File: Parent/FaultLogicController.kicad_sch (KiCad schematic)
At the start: 4 parts, among them U57 4072, U60 4071

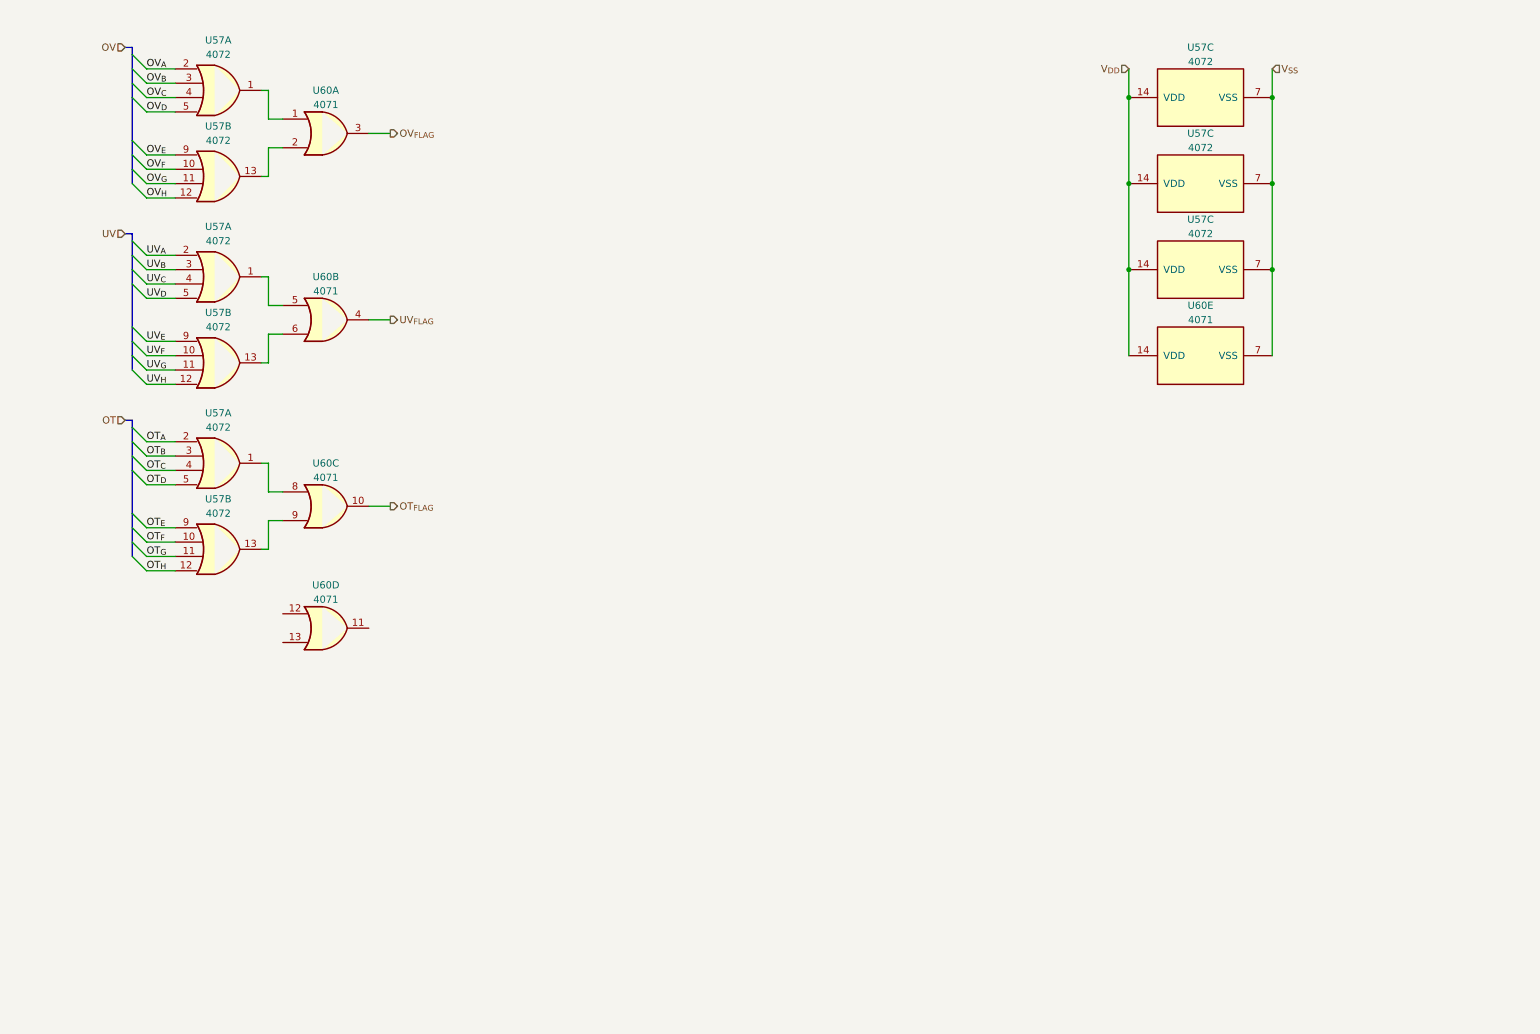
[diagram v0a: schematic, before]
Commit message: Updated Parent further - Move workspace to cloud
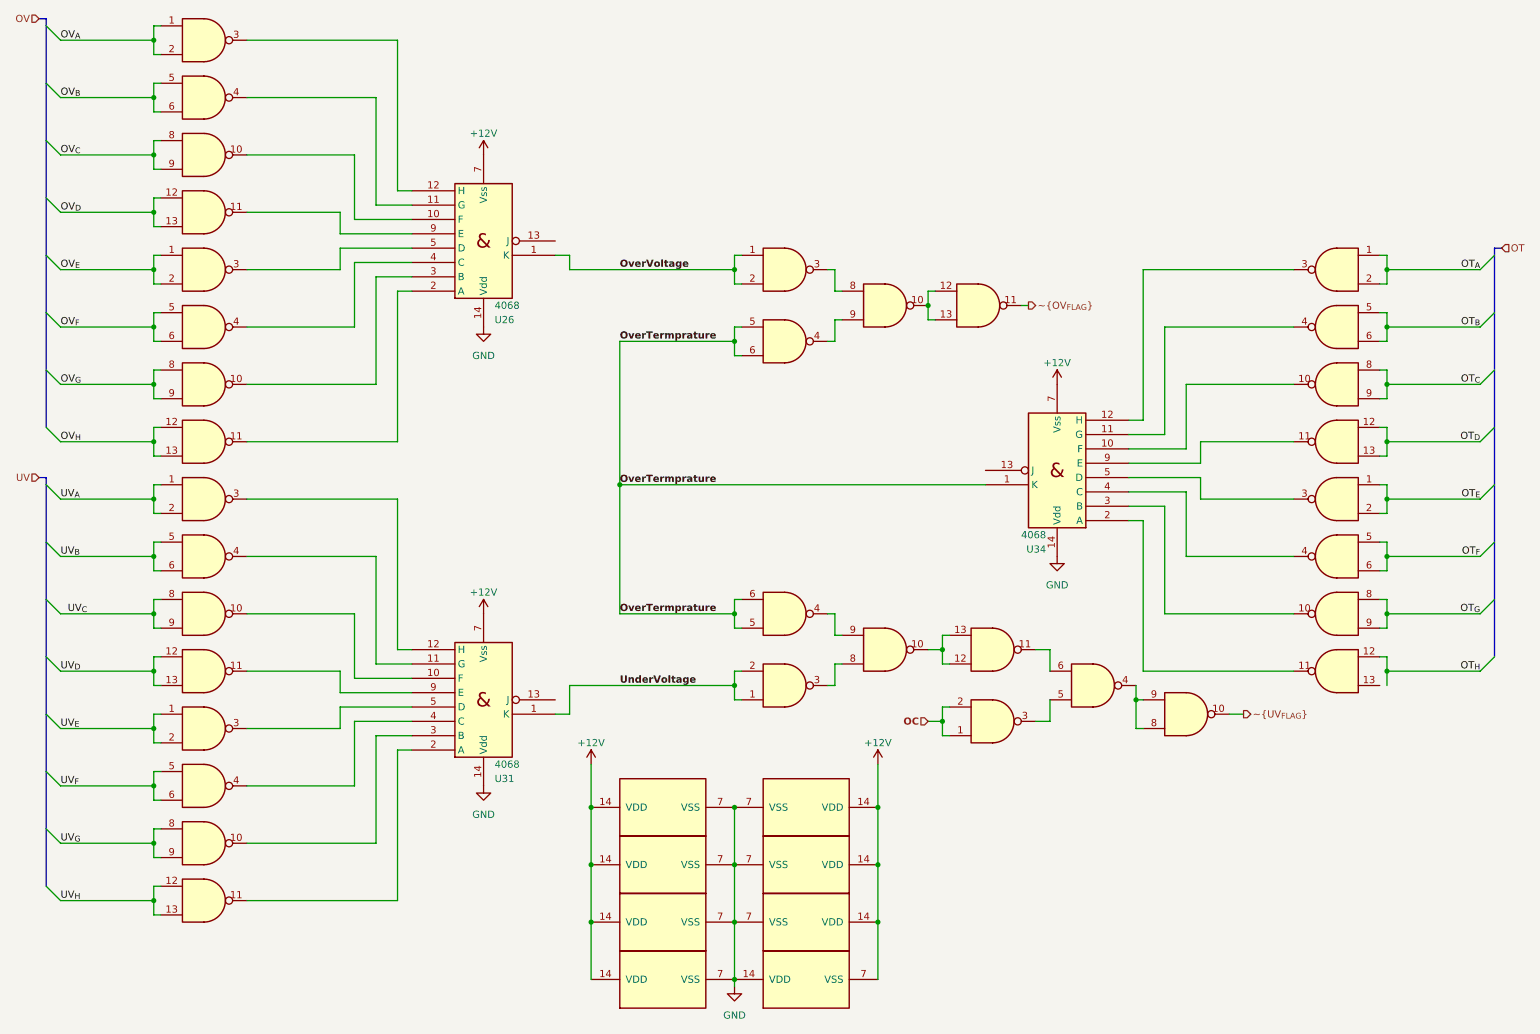
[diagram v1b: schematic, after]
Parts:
- removed U57 (x3): 4072, symbol 4xxx:4072
- removed U60: 4071, symbol 4xxx:4071
- added U15, U16, U20, U21, U23, U28, U29, U57 (x2): 4011, symbol 4xxx:4011
- added U26, U31, U34: 4068, symbol 4xxx_IEEE:4068
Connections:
- net OT_{A}: now also U28.1, U28.2
- net OT_{B}: now also U28.5, U28.6
- net OT_{C}: now also U28.8, U28.9
- net OT_{D}: now also U28.12, U28.13
- net OT_{E}: now also U29.1, U29.2
- net OT_{F}: now also U29.5, U29.6
- net OT_{G}: now also U29.8, U29.9
- net OT_{H}: now also U29.12
- net OV_{A}: now also U20.1, U20.2
- net OV_{B}: now also U20.5, U20.6
- net OV_{C}: now also U20.8, U20.9
- net OV_{D}: now also U20.12, U20.13
- net OV_{E}: now also U21.1, U21.2
- net OV_{F}: now also U21.5, U21.6
- net OV_{G}: now also U21.8, U21.9
- net OV_{H}: now also U21.12, U21.13
- net UV_{A}: now also U15.1, U15.2
- net UV_{B}: now also U15.5, U15.6
- net UV_{C}: now also U15.8, U15.9
- net UV_{D}: now also U15.12, U15.13
- net UV_{E}: now also U16.1, U16.2
- net UV_{F}: now also U16.5, U16.6
- net UV_{G}: now also U16.8, U16.9
- net UV_{H}: now also U16.12, U16.13
- new net: U20.4, U26.11 (G)
- new net: U20.3, U26.12 (H)
- new net: U29.3, U34.5 (D)
- new net: U23.10, U23.12, U23.13
- new net: U23.3, U23.8
- new net: U23.4, U23.9
- new net: U28.4, U34.11 (G)
- new net: U20.10, U26.10 (F)
- new net: U21.11, U26.2 (A)
- new net: U21.10, U26.3 (B)
- new net: U21.4, U26.4 (C)
- new net: U21.3, U26.5 (D)
- new net: U20.11, U26.9 (E)
- new net: U57.4, U57.8, U57.9
- new net: U16.10, U31.3 (B)
- new net: U28.3, U34.12 (H)
- new net: U57.3, U57.5
- new net: U57.11, U57.6
- new net: U57.10, U57.12, U57.13
- new net: U16.11, U31.2 (A)
- new net: U16.4, U31.4 (C)
- new net: U15.10, U31.10 (F)
- new net: U15.4, U31.11 (G)
- new net: U15.3, U31.12 (H)
- new net: U16.3, U31.5 (D)
- new net: U15.11, U31.9 (E)
- new net: U57.3, U57.8
- new net: U29.4, U34.4 (C)
- new net: U29.11, U34.2 (A)
- new net: U29.10, U34.3 (B)
- new net: U57.4, U57.9
- new net: U28.10, U34.10 (F)
- new net: U28.11, U34.9 (E)
- new net +12V: U15.14 (VDD), U16.14 (VDD), U20.14 (VDD), U20.14 (VDD), U20.7 (VSS), U21.14 (VDD), U23.14 (VDD), U26.7 (Vss), U28.14 (VDD), U31.7 (Vss), U34.7 (Vss)
- new net GND: U15.7 (VSS), U16.7 (VSS), U20.14 (VDD), U20.7 (VSS), U20.7 (VSS), U21.7 (VSS), U23.7 (VSS), U26.14 (Vdd), U28.7 (VSS), U31.14 (Vdd), U34.14 (Vdd)
- new net OC: U57.1, U57.2
- new net OverTermprature: U23.5, U23.6, U34.1 (K), U57.5, U57.6
- new net OverVoltage: U23.1, U23.2, U26.1 (K)
- new net UnderVoltage: U31.1 (K), U57.1, U57.2
- new net ~{OV_{FLAG}}: U23.11
- new net ~{UV_{FLAG}}: U57.10

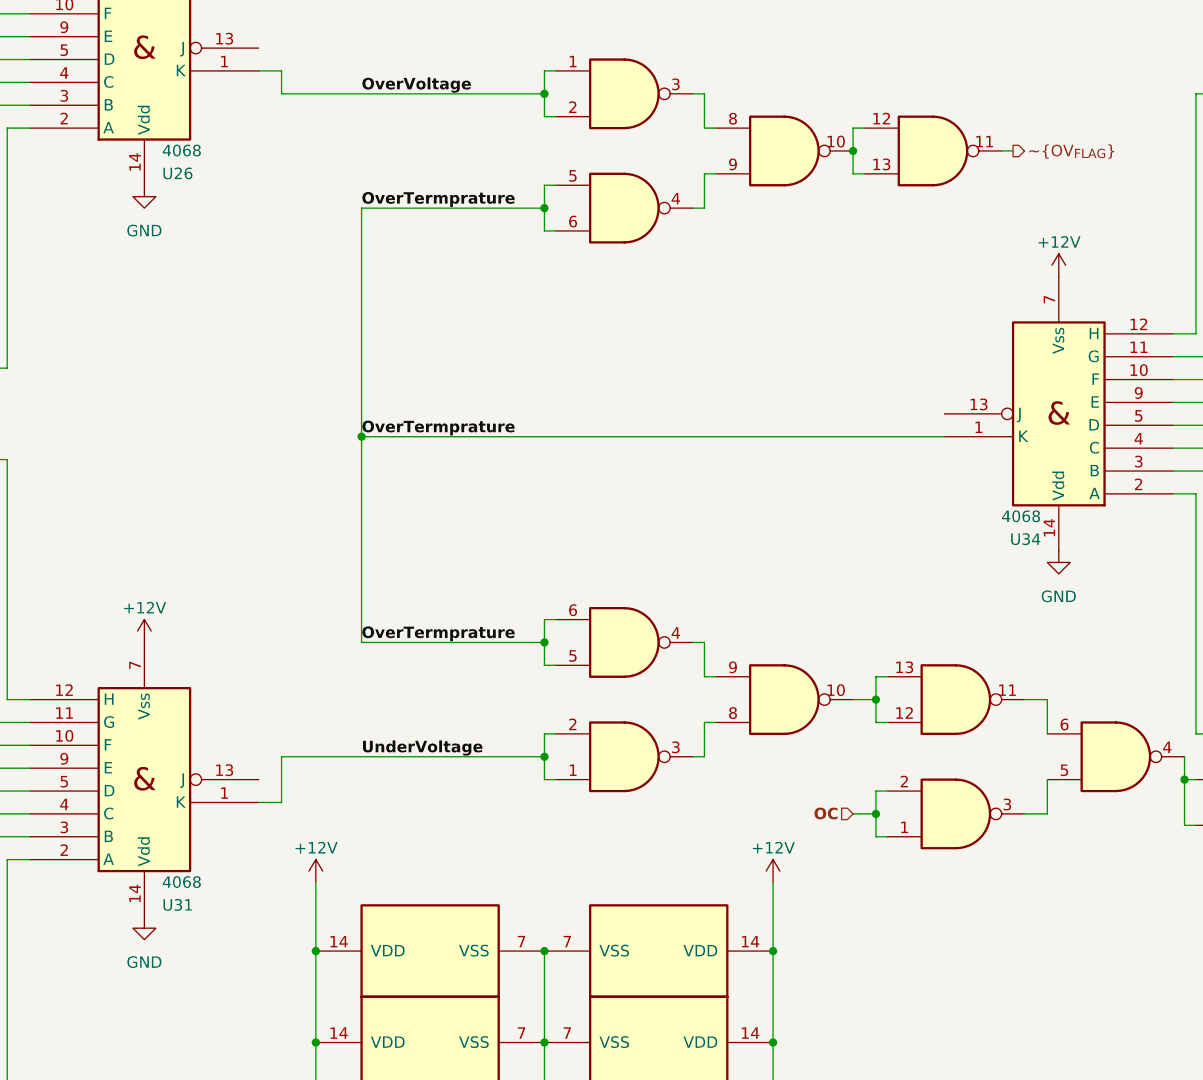
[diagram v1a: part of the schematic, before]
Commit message: Updated Parent further - Move workspace to cloud
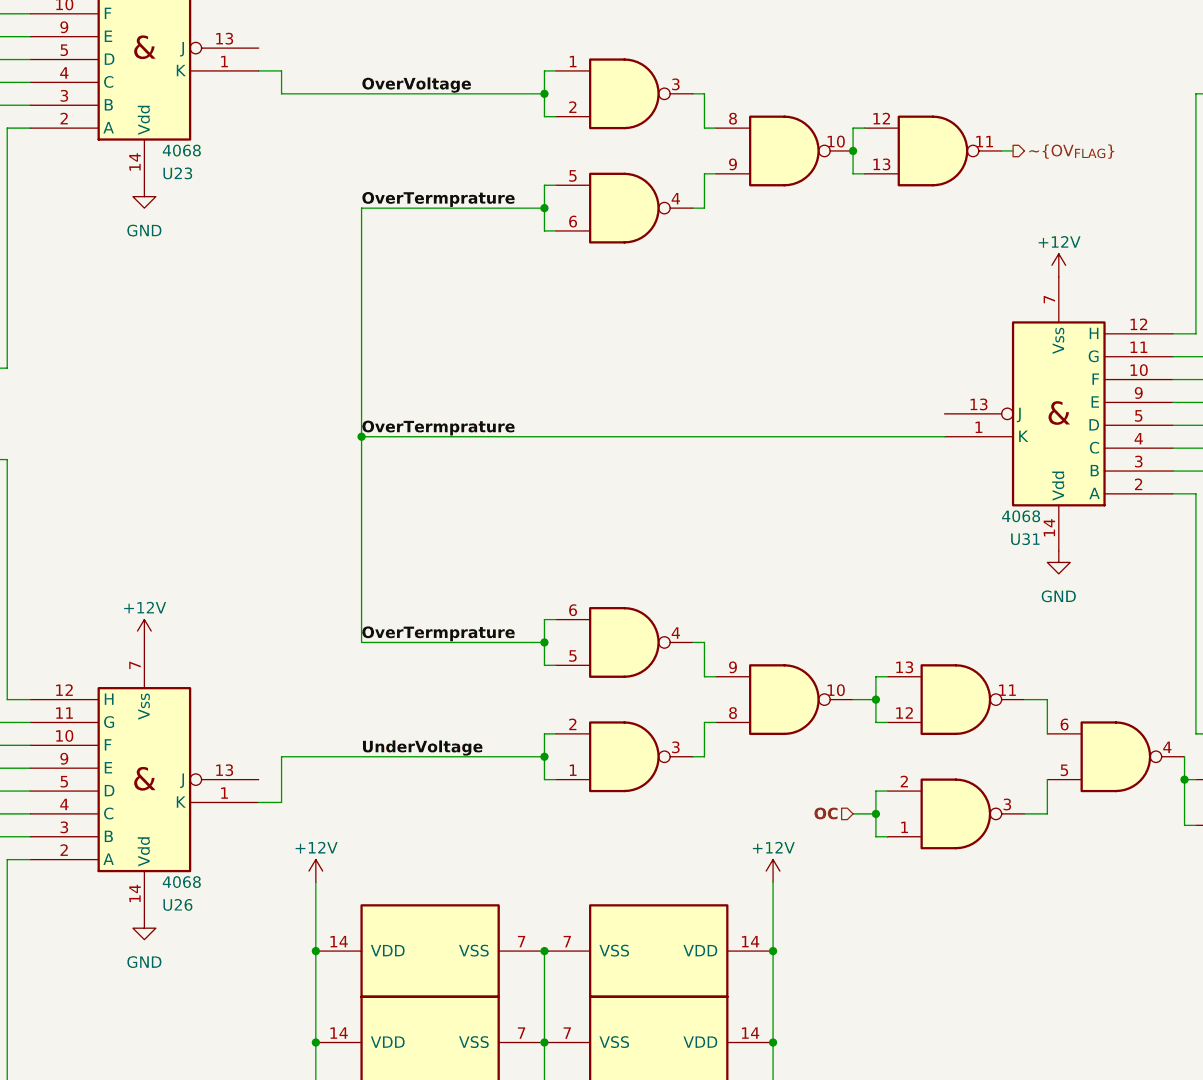
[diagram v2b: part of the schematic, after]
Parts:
- renumbered U20 to U15, U21 to U16, U15 to U20, U16 to U21, U26 to U23, U31 to U26, U23 to U28, U57 to U29, U20 to U29, U34 to U31, U28 to U34, U29 to U57, U20 to U57, U57 to U58, U57 to U59

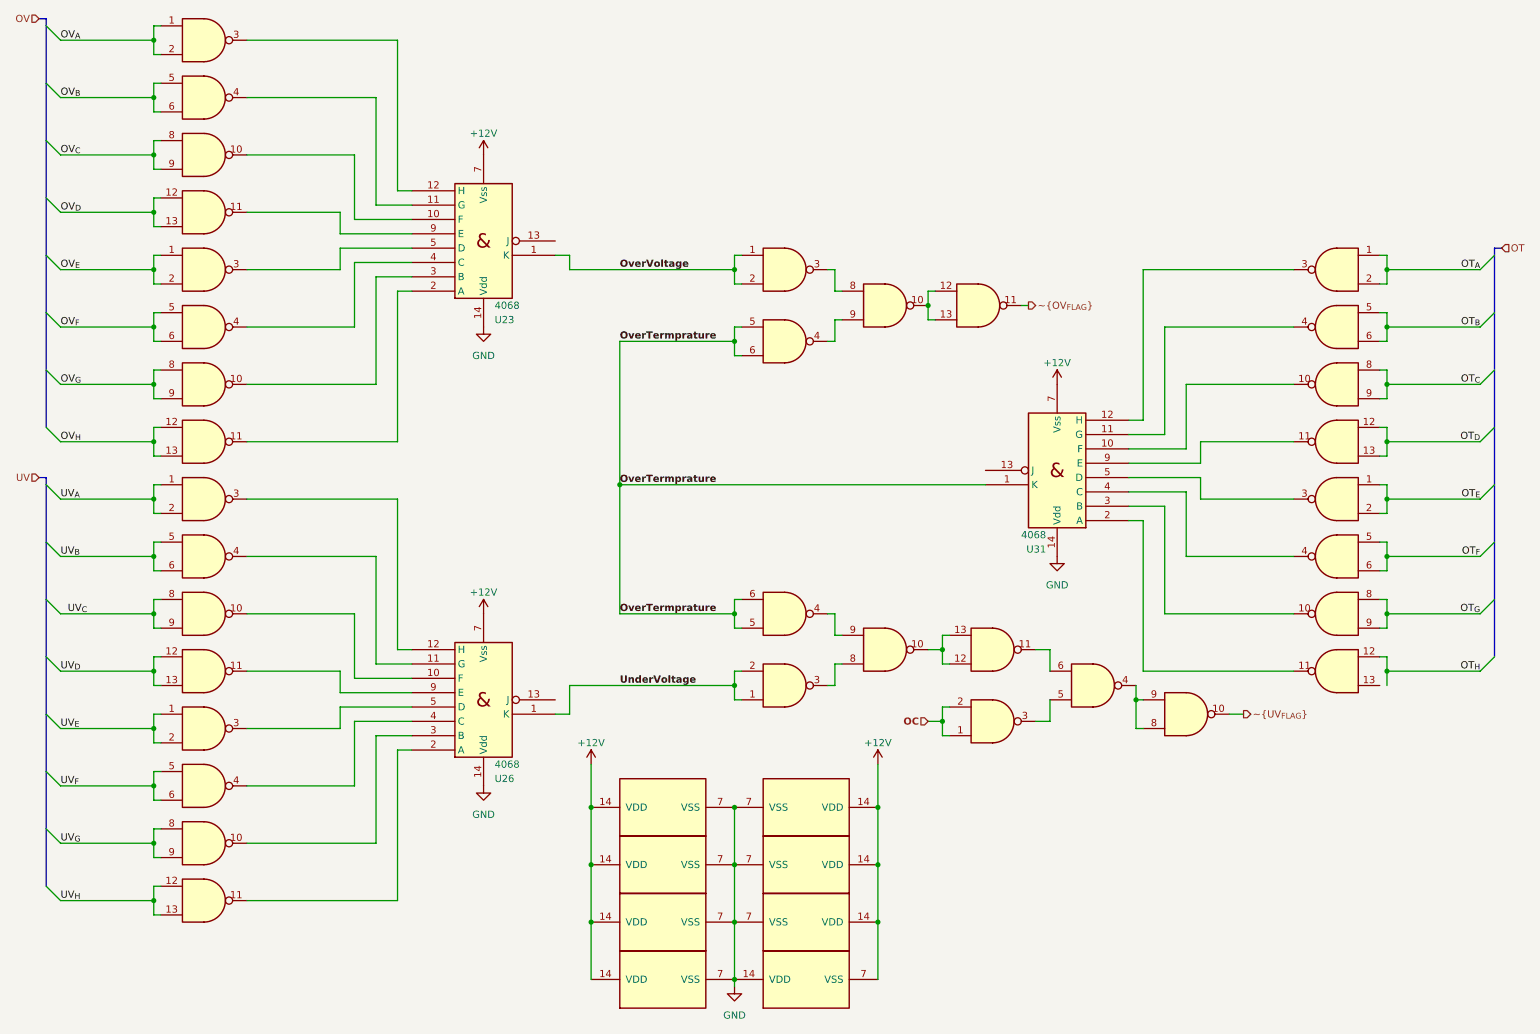
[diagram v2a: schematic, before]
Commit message: Updated Parent - Moved workspace to cloud
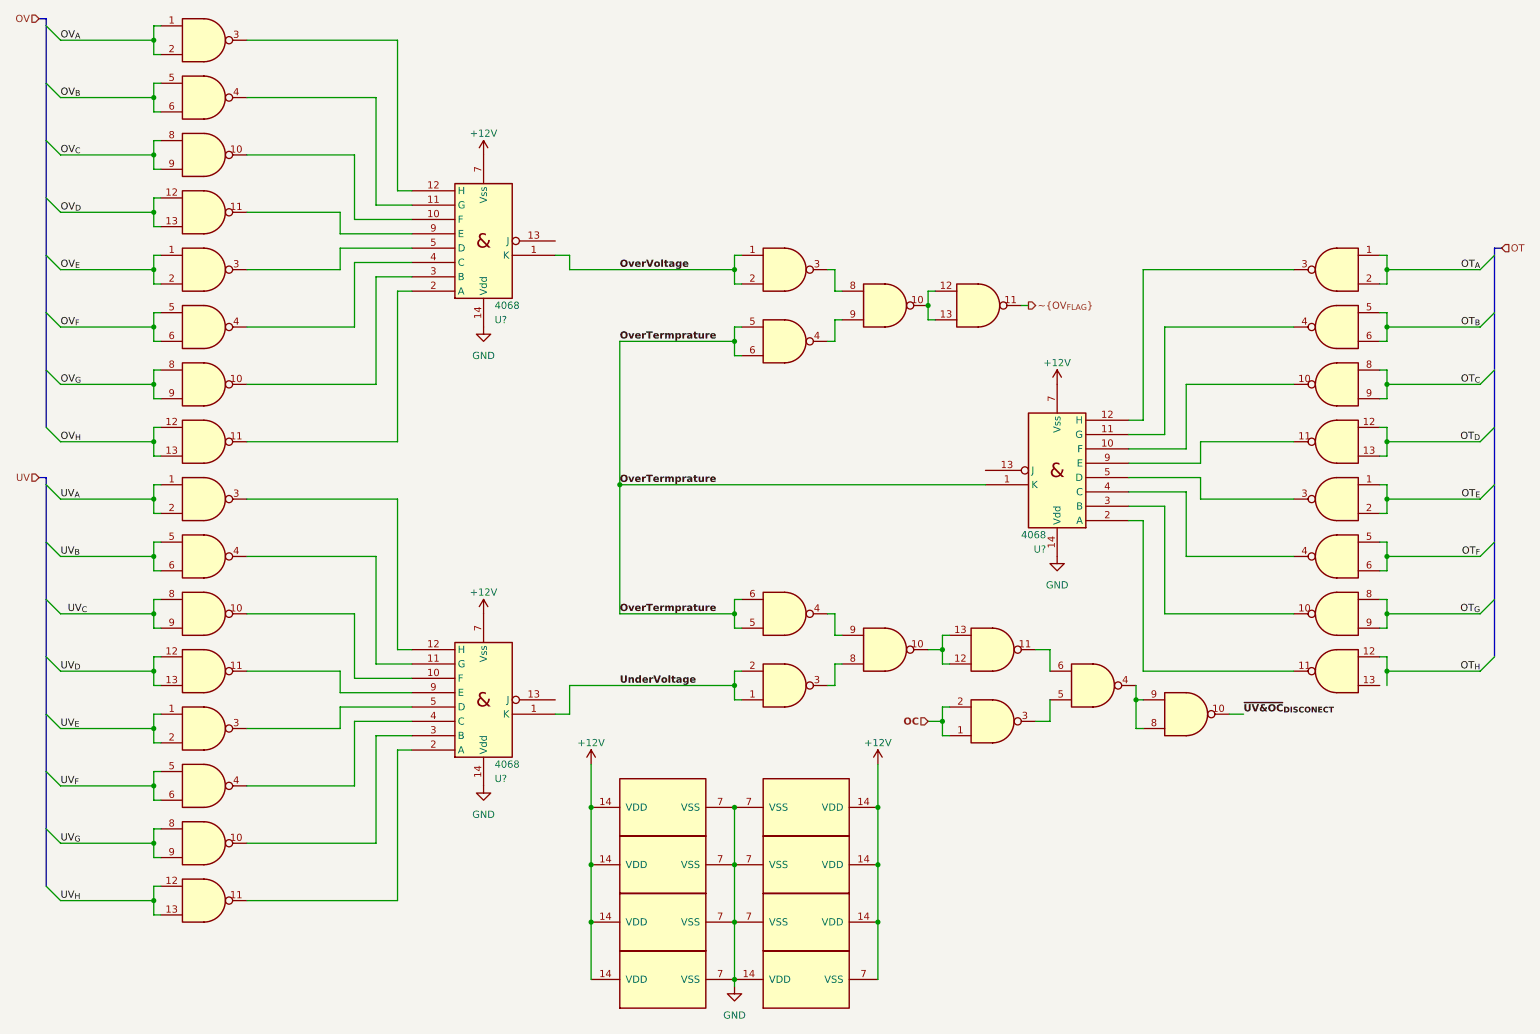
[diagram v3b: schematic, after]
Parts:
- renumbered U15 to U?, U16 to U?, U57 to U?, U28 to U?, U34 to U?, U23 to U?, U58 to U?, U21 to U?, U59 to U?, U20 to U?, U26 to U?, U29 to U?, U31 to U?
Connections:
- net ~{UV_{FLAG}} renamed ~{UV&OC}_{DISCONECT}
